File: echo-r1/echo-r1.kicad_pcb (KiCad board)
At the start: 6 copper layers, 55 x 95 mm, 154 parts, among them J1 GT-BTP30003-xxxA-16A, J2 TYPE-C-31-M-12, J3 TF-115, J4 HP_3.5mm, J5 LO_3.5mm, J6 AFD01-S35FCC-00, J7 PM254-1-06-W-8.5, Q2 AO3401A, Q5 AO3401A, Q6 AO3401A, Q7 AO3401A, SW1 DPAD↑, SW10 X, SW11 Y, SW12 START, SW13 SELECT, SW14 HOLD, SW2 DPAD↓, SW3 DPAD←, SW4 DPAD→, SW5 A, SW6 B, SW7 VOL+, SW8 VOL-, SW9 POWER, U1 LM66100DCK, U10 SY7200A, U2 TPS62A01DRLR, U3 TPS62A01DRLR, U4 XC6206P33xMR, U5 TP4057, U6 STM32H743IGTx, U7 W9825G6KH-x, U8 USB3320C-EZK, U9 TLV320AIC3104, Y1 SC-32S32.768kHz20PPM12.5pF, Y2 XTM32024000JT00351001

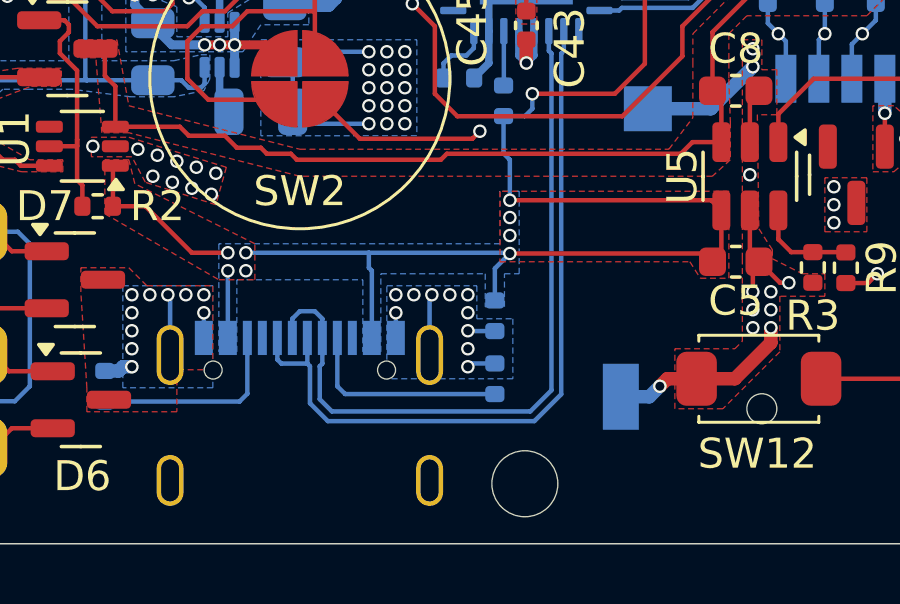
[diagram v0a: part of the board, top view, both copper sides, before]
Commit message: R1-Rev1: remove VBUS discharge resistor
This is not needed since there is a path through the ADC
voltage divider to discharge VBUS -- and realistically
the battery charger should also discharge VBUS even with
no resistive path to ground.
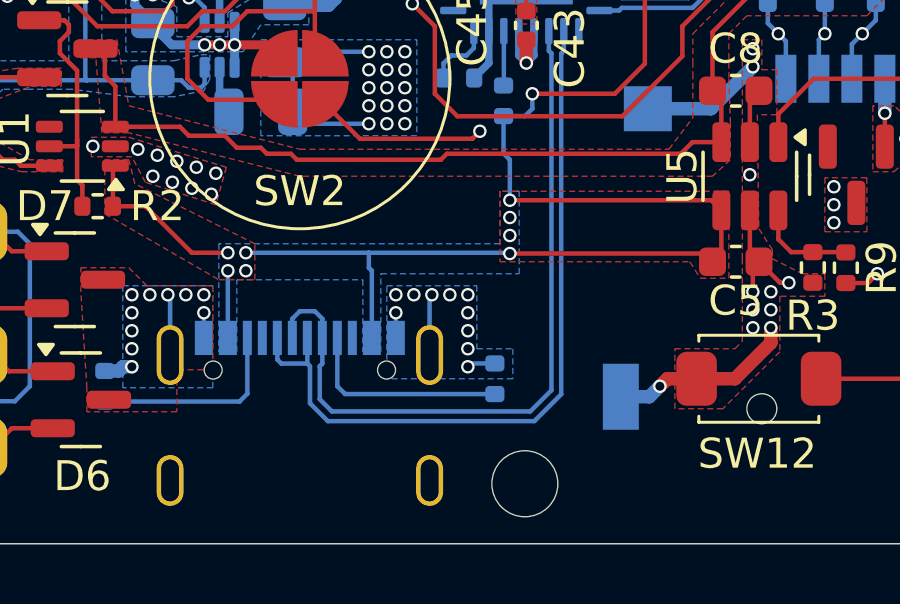
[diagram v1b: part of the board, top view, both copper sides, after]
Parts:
- removed R13: 100 kΩ, Resistor_SMD:R_0402_1005Metric
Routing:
- net VBUS: track 152.7 -> 151.0 mm
- net GND: track 207.1 -> 206.2 mm

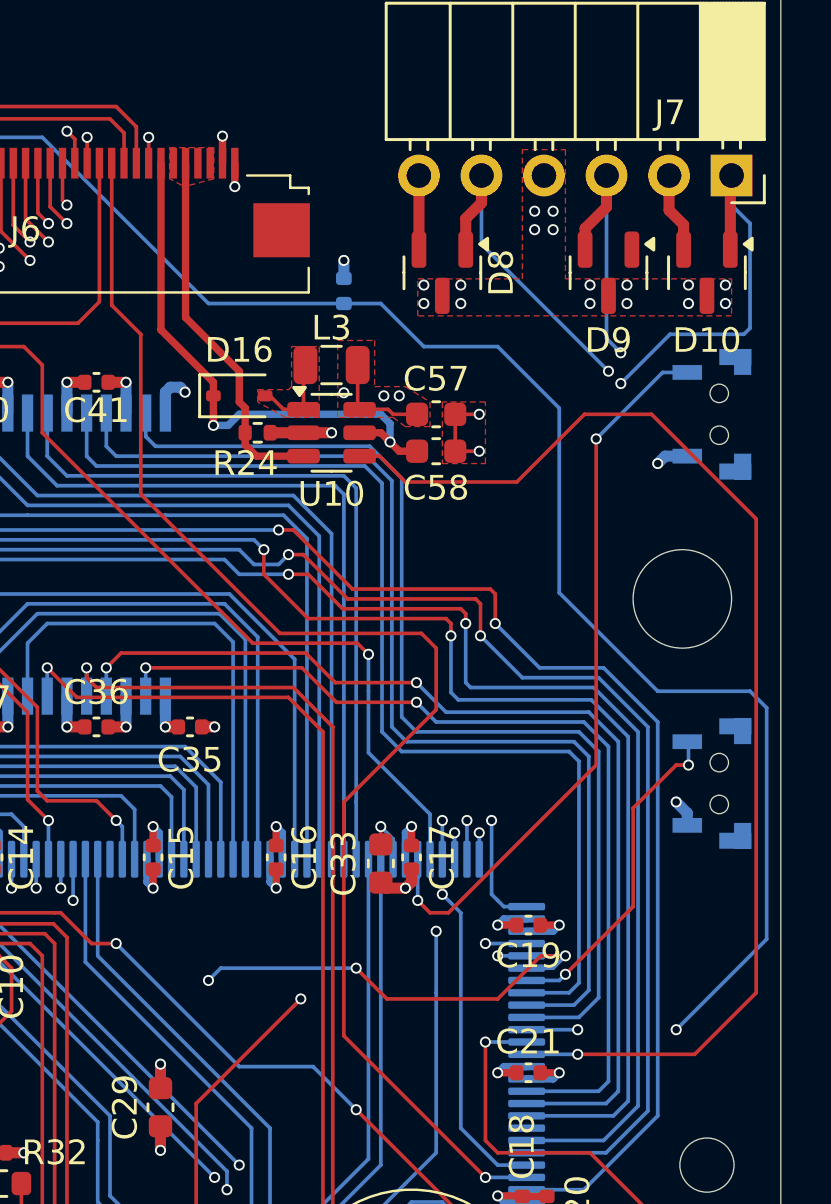
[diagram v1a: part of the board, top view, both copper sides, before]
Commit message: R1-Rev1: replace SY7200A LED driver with AP2502 current limiter
The SY7200A is a boost converter designed for series LED
strings, which require a high drive voltage. The external
circuitry allows some input power to pass through to the
output -- which is normally not a problem for LED strings
because this low voltage is not enough to overcome their
combined voltage drop.

However, the LCD uses 4 LEDs in parallel, and this low
voltage is enough to light the LEDs while the converter
is disabled, so the backlight can't be turned off.

Fix this by using the AP2502 4-channel current limiter
instead, which is basically a low side switch. LEDs are
powered directly from 3.3V, and each is independently
switched through the AP2502.
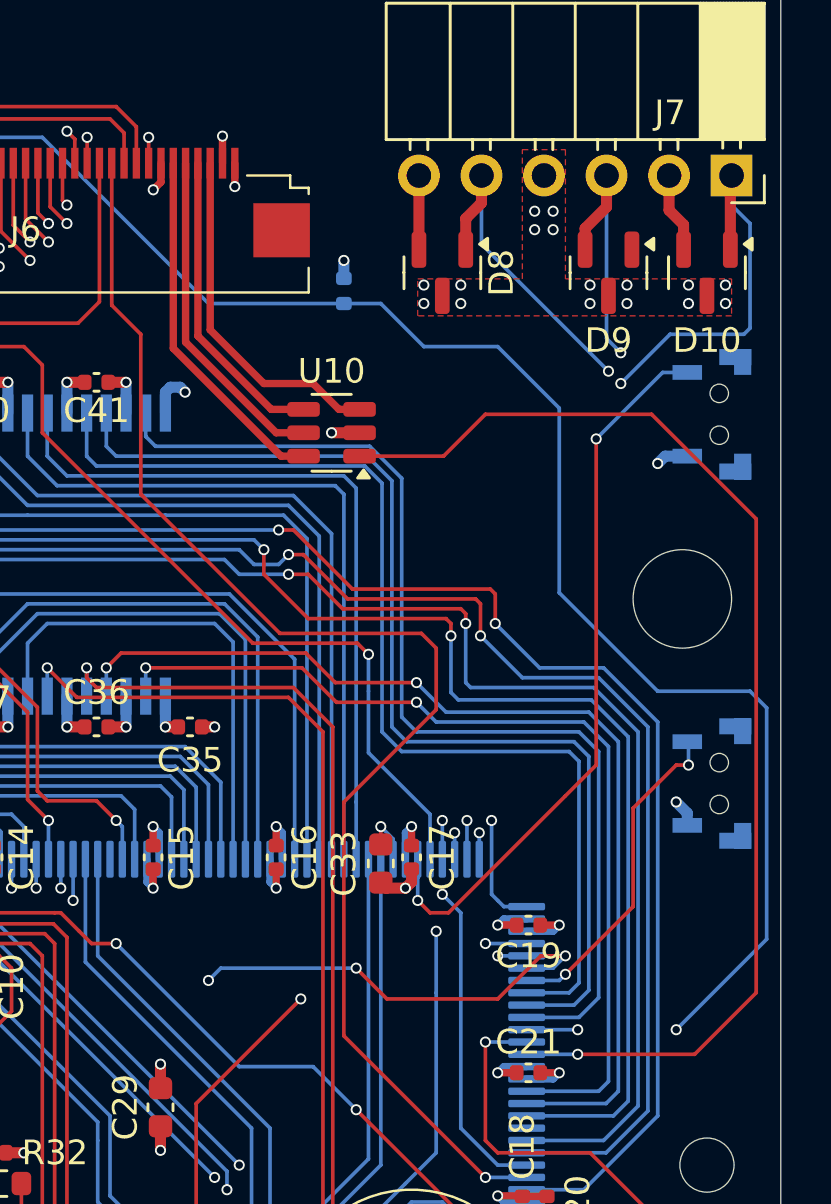
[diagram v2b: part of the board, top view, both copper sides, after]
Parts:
- removed C57, C58: 4.7 µF, Capacitor_SMD:C_0603_1608Metric
- removed D16: 1N5819WS, Diode_SMD:D_SOD-323
- removed L3: 4.7 µH, echoplayer:L_0806_2016Metric
- removed R24: 10 Ω, Resistor_SMD:R_0402_1005Metric
- U10: value SY7200A -> AP2502
- turned U10 to 180 degrees
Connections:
- J6 pad 29: /lcd/led_a -> 3V3
- J6 pad 30: /lcd/led_k -> /lcd/led_k1
- J6 pad 31: /lcd/led_k -> /lcd/led_k2
- J6 pad 32: /lcd/led_k -> /lcd/led_k3
- J6 pad 33: /lcd/led_k -> /lcd/led_k4
- U10 pad 1: /lcd/led_driver_lx -> /cpu/backlight_pwm
- U10 pad 3: /lcd/led_k -> /lcd/led_k4
- U10 pad 4: /cpu/backlight_pwm -> /lcd/led_k3
- U10 pad 5: /lcd/led_a -> /lcd/led_k2
- U10 pad 6: 3V3 -> /lcd/led_k1
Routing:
- net /lcd/led_a: track 22.4 -> 0.00 mm, vias 2 -> 0
- net /lcd/led_k: track 15.0 -> 0.00 mm
- net /lcd/led_k1: track 0.00 -> 14.6 mm
- net /lcd/led_k4: track 0.00 -> 14.3 mm
- net /lcd/led_k2: track 0.00 -> 13.6 mm
- net /lcd/led_k3: track 0.00 -> 12.5 mm
- net GND: track 206.2 -> 201.4 mm, vias 190 -> 188
- net /lcd/led_driver_lx: track 3.69 -> 0.00 mm
- net 3V3: track 89.8 -> 86.7 mm, vias 56 -> 54
- net /cpu/backlight_pwm: track 49.1 -> 48.2 mm
- removed copper zone on F.Cu, net /lcd/led_driver_lx
- removed copper zone on F.Cu, net /lcd/led_k

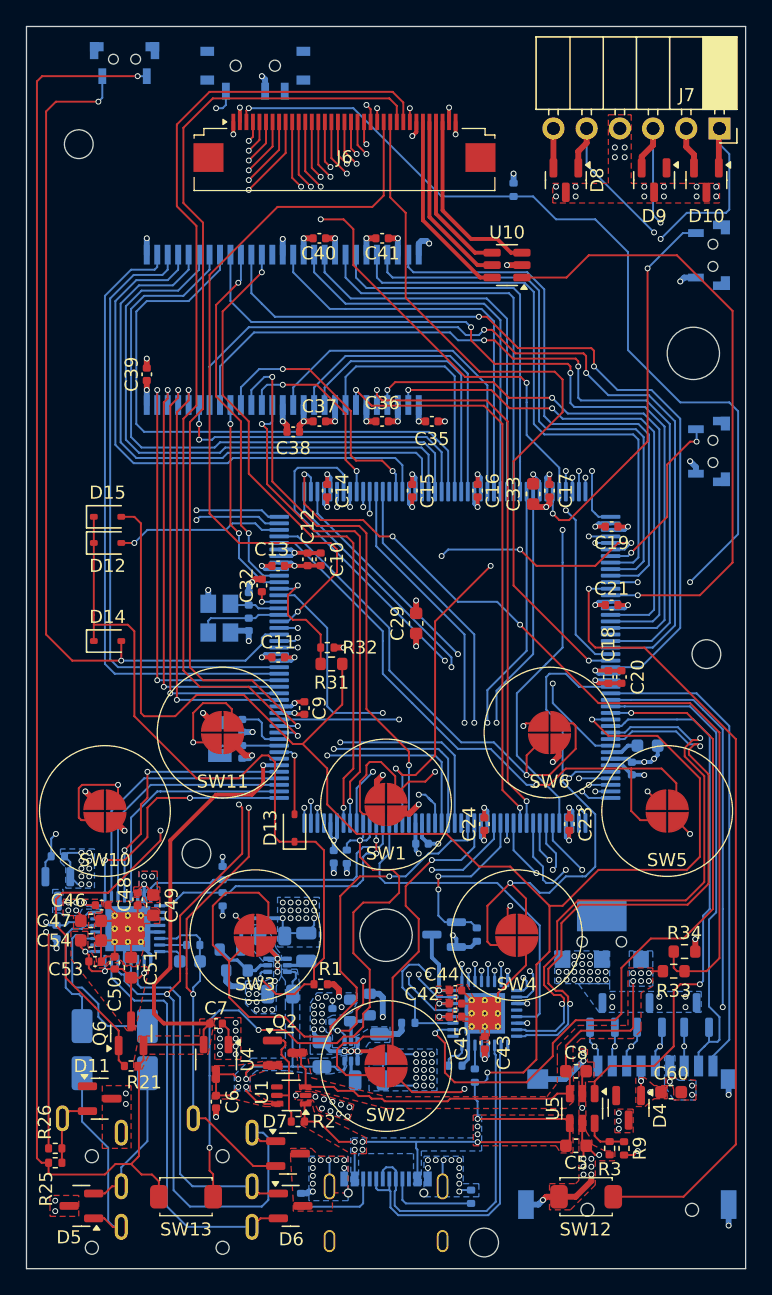
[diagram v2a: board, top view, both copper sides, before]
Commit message: WIP redesign with STM32H7R3Z8J6
The H7R3 has a bunch of features that greatly simplify the design:
support for HyperRAM, which requires far fewer pins than SDRAM and
is more power efficient; this frees up the FMC to interface with the
display in 8-bit 8080 MCU mode; and there is a built-in USB HS PHY,
removing the need for an external PHY.

The huge reduction in signal count allows for a smaller pin count
package -- only 144 pins. HyperRAM only comes in BGA packages so it
makes sense to also use the UFBGA-144 package for the CPU, which
takes up less than 1/4 of the board area of an LQFP-176 package.
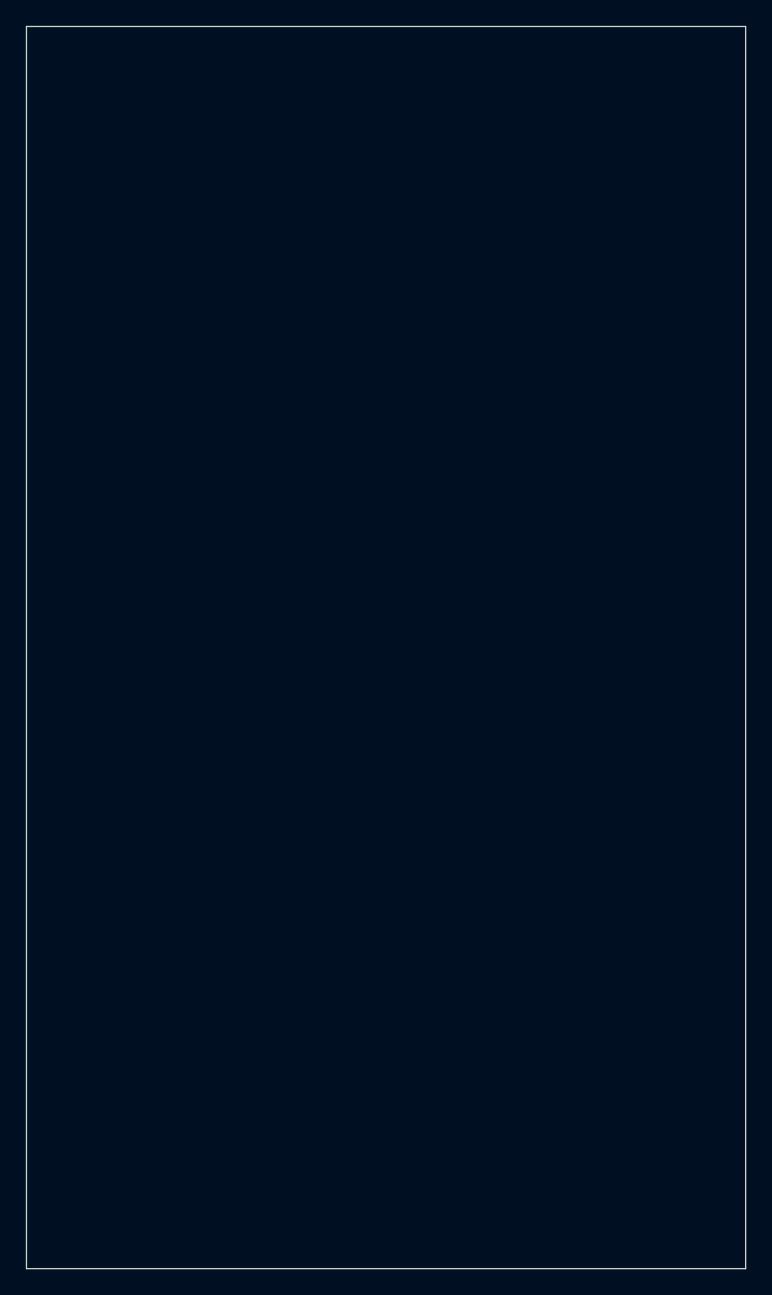
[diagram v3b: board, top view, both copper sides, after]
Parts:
- removed C1, C2, C3, C4: 22 µF, Capacitor_SMD:C_0805_2012Metric
- removed C10, C11, C13, C14, C15, C16, C17, C18, C19, C21, C22, C23, C24, C25, C26, C32, C35, C36, C37, C38, C39, C40, C41, C42, C43, C44, C45, C46, C48, C50, C53, C9: 100 nF, Capacitor_SMD:C_0402_1005Metric
- removed C12, C20, C6, C7: 1 µF, Capacitor_SMD:C_0402_1005Metric
- removed C27, C30: 5 pF/NP0, Capacitor_SMD:C_0402_1005Metric
- removed C28, C31: 4 pF/NP0, Capacitor_SMD:C_0402_1005Metric
- removed C29, C5, C8: 4.7 µF, Capacitor_SMD:C_0603_1608Metric
- removed C33, C34: 2.2 µF, Capacitor_SMD:C_0603_1608Metric
- removed C47, C49, C51, C54, C60: 10 µF, Capacitor_SMD:C_0603_1608Metric
- removed C52: 10 nF/NP0, Capacitor_SMD:C_0603_1608Metric
- removed C55, C56: 10 µF, Capacitor_SMD:CP_Elec_4x5.4
- removed D1, D10, D11, D2, D3, D4, D6, D7, D8, D9: CESD3V3AP-ES, Package_TO_SOT_SMD:SOT-23
- removed D12, D13, D14, D15: 1N5819WS, Diode_SMD:D_SOD-323
- removed D5: PESD3V3L2BT, Package_TO_SOT_SMD:SOT-23
- removed H1: DPad_Pivot, MountingHole:MountingHole_4mm
- removed H2: Volume_Pivot, MountingHole:MountingHole_4mm
- removed H3, H4, H5, H6: M2_Screw, MountingHole:MountingHole_2.2mm_M2
- removed J1: GT-BTP30003-xxxA-16A, echoplayer:Conn_GT-BTP30003-xxxxA-016A
- removed J2: TYPE-C-31-M-12, echoplayer:USB_C-Hroparts-TYPE-C-31-M-12
- removed J3: TF-115, echoplayer:microSD_XUNPU_TF-115
- removed J4: HP_3.5mm, echoplayer:Jack_3.5mm_HCTL_HC-PJ-320A-4P-D
- removed J5: LO_3.5mm, echoplayer:Jack_3.5mm_HCTL_HC-PJ-320A-4P-D
- removed J6: AFD01-S35FCC-00, echoplayer:Conn_Jushuo_AFD01-S35FCC-00_RTL
- removed J7: PM254-1-06-W-8.5, Connector_PinSocket_2.54mm:PinSocket_1x06_P2.54mm_Horizontal
- removed L1, L2: 1 µH, echoplayer:L_0806_2016Metric
- removed NT1, NT2: NetTie_2, echoplayer:NetTie_0.15mm_SMD
- removed Q2, Q5, Q6, Q7: AO3401A, Package_TO_SOT_SMD:SOT-23
- removed R1, R10, R18, R19, R2, R20, R21, R22, R26, R30, R32, R4: 100 kΩ, Resistor_SMD:R_0402_1005Metric
- removed R11, R12, R16, R3: 10 kΩ, Resistor_SMD:R_0402_1005Metric
- removed R14, R15: 5.1 kΩ, Resistor_SMD:R_0402_1005Metric
- removed R17: 8.06 kΩ, Resistor_SMD:R_0402_1005Metric
- removed R23, R9: 2.2 kΩ, Resistor_SMD:R_0402_1005Metric
- removed R25: 1 MΩ, Resistor_SMD:R_0402_1005Metric
- removed R31, R33, R5: 174 kΩ, Resistor_SMD:R_0603_1608Metric
- removed R34, R7: 390 kΩ, Resistor_SMD:R_0603_1608Metric
- removed R6, R8: 86.6 kΩ, Resistor_SMD:R_0603_1608Metric
- removed SW1: DPAD↑, echoplayer:Switch_ContactPad_10x3mm_Cross
- removed SW10: X, echoplayer:Switch_ContactPad_10x3mm_Cross
- removed SW11: Y, echoplayer:Switch_ContactPad_10x3mm_Cross
- removed SW12: START, echoplayer:Switch_XUNPU_TS-1088-AR
- removed SW13: SELECT, echoplayer:Switch_XUNPU_TS-1088-AR
- removed SW14: HOLD, echoplayer:Switch_SHOUHAN_MSK12C02-HB
- removed SW2: DPAD↓, echoplayer:Switch_ContactPad_10x3mm_Cross
- removed SW3: DPAD←, echoplayer:Switch_ContactPad_10x3mm_Cross
- removed SW4: DPAD→, echoplayer:Switch_ContactPad_10x3mm_Cross
- removed SW5: A, echoplayer:Switch_ContactPad_10x3mm_Cross
- removed SW6: B, echoplayer:Switch_ContactPad_10x3mm_Cross
- removed SW7: VOL+, echoplayer:Switch_XKB_TS-1010-C-A
- removed SW8: VOL-, echoplayer:Switch_XKB_TS-1010-C-A
- removed SW9: POWER, echoplayer:Switch_XKB_TS-1010-C-A
- removed U1: LM66100DCK, Package_TO_SOT_SMD:Texas_R-PDSO-G6
- removed U10: AP2502, Package_TO_SOT_SMD:SOT-23-6
- removed U2, U3: TPS62A01DRLR, Package_TO_SOT_SMD:SOT-563
- removed U4: XC6206P33xMR, Package_TO_SOT_SMD:SOT-23-3
- removed U5: TP4057, Package_TO_SOT_SMD:TSOT-23-6
- removed U6: STM32H743IGTx, Package_QFP:LQFP-176_24x24mm_P0.5mm
- removed U7: W9825G6KH-x, Package_SO:TSOP-II-54_22.2x10.16mm_P0.8mm
- removed U8: USB3320C-EZK, Package_DFN_QFN:QFN-32-1EP_5x5mm_P0.5mm_EP3.1x3.1mm_ThermalVias
- removed U9: TLV320AIC3104, Package_DFN_QFN:Texas_RHB0032E_VQFN-32-1EP_5x5mm_P0.5mm_EP3.45x3.45mm_ThermalVias
- removed Y1: SC-32S32.768kHz20PPM12.5pF, Crystal:Crystal_SMD_3215-2Pin_3.2x1.5mm
- removed Y2: XTM32024000JT00351001, Crystal:Crystal_SMD_3225-4Pin_3.2x2.5mm
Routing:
- net GND: track 201.4 -> 0.00 mm, vias 188 -> 0
- net VBUS: track 151.0 -> 0.00 mm, vias 10 -> 0
- net 3V3_LDO: track 149.1 -> 0.00 mm, vias 2 -> 0
- net /cpu/swd_nrst: track 93.0 -> 0.00 mm, vias 1 -> 0
- net 3V3: track 86.7 -> 0.00 mm, vias 54 -> 0
- net /cpu/lcd_rgb.vsync: track 75.3 -> 0.00 mm, vias 1 -> 0
- net /cpu/swd_swo: track 73.8 -> 0.00 mm, vias 3 -> 0
- net /cpu/~{lcd_reset}: track 73.2 -> 0.00 mm, vias 3 -> 0
- net /cpu/lcd_rgb.hsync: track 72.5 -> 0.00 mm, vias 1 -> 0
- net /button/button_hold: track 68.4 -> 0.00 mm, vias 3 -> 0
- net /button/button_power: track 67.7 -> 0.00 mm, vias 2 -> 0
- net /cpu/lcd_rgb.g5: track 67.4 -> 0.00 mm, vias 2 -> 0
- net /cpu/lcd_rgb.g4: track 65.6 -> 0.00 mm, vias 2 -> 0
- net /cpu/adc_vbat: track 65.4 -> 0.00 mm, vias 3 -> 0
- net /cpu/swd_clk: track 65.4 -> 0.00 mm, vias 2 -> 0
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- removed copper zone on F.Cu, net /audio/avdd
- removed copper zone on B.Cu, net /audio/dvdd
- removed copper zone on F.Cu, net /audio/dvdd
- removed copper zone on B.Cu, net /power/power_vsys
- removed copper zone on F.Cu, net /power/power_vsys
- removed copper zone on F.Cu, net /usb/power_io_sw
- removed copper zone on B.Cu, net 1V8
- removed copper zone on F.Cu, net 1V8
- removed copper zone on In3.Cu, net 1V8
- removed copper zone on B.Cu, net 3V3
- removed copper zone on F.Cu, net 3V3
- removed copper zone on F.Cu, net 3V3_LDO
- removed copper zone on B.Cu, net GND
- removed copper zone on F.Cu, net GND
- removed copper zone on B.Cu, net VBAT
- removed copper zone on F.Cu, net VBAT
- removed copper zone on B.Cu, net VBUS
- removed copper zone on F.Cu, net VBUS
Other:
- board text removed: "ACTIVE AREA"
- board text removed: "BATTERY"
- board text removed: "COVER AREA"
- board text removed: "Cable length shortened by 1.2mm to account for bending"
- board text removed: "JLCJLCJLCJLC"
- board text removed: "MODULE OUTLINE"
- board text removed: "QR"

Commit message: Continue with redesign, update and simplify schematic
- Consolidate small sheets (ports, etc) onto one page
- Add placeholders for STM32 external components
- Add power switch on SD card for resetting it
- Fix oversized input capacitors on voltage regulators
- Get rid of unique 1M resistor used in line-out detection
- Remove SOT23 TVS diodes (will be replaced by another package)
- Update LCD connector symbol for new 30pin screen
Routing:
- added copper zone on In2.Cu, net (none)
- removed copper zone on In2.Cu, net 3V3
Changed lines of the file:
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@@
 	(net 0 "")
 	(net 1 "GND")
-	(net 2 "3V3")
 	(gr_rect
 		(start 118.5 55)
@@
 	)
 	(zone
-		(net 2)
-		(net_name "3V3")
+		(net 0)
+		(net_name "")
 		(layer "In2.Cu")
 		(hatch edge 0.5)
